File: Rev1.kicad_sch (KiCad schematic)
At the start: 105 parts, among them J1 Conn_01x08_Socket, J10 Conn_01x08_Socket, J11 Conn_01x02_Socket, J12 Conn_01x08_Socket, J13 Conn_01x08_Socket, J2 Conn_01x08_Socket, J3 Conn_01x08_Socket, J4 Conn_01x08_Socket, J5 Conn_01x08_Socket, J6 Conn_01x08_Socket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

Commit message: Update, pics
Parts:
- J11: value Conn_01x02_Socket -> Power
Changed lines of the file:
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@@
 		(on_board yes)
 		(dnp no)
-		(fields_autoplaced yes)
 		(property "Reference" "J11"
 			(at 21.59 30.4799 0)
@@
 			)
 		)
-		(property "Value" "Conn_01x02_Socket"
-			(at 21.59 31.7499 0)
+		(property "Value" "Power"
+			(at 22.098 33.274 0)
 			(effects
 				(font
@@
 				)
 				(justify left)
-				(hide yes)
 			)
 		)

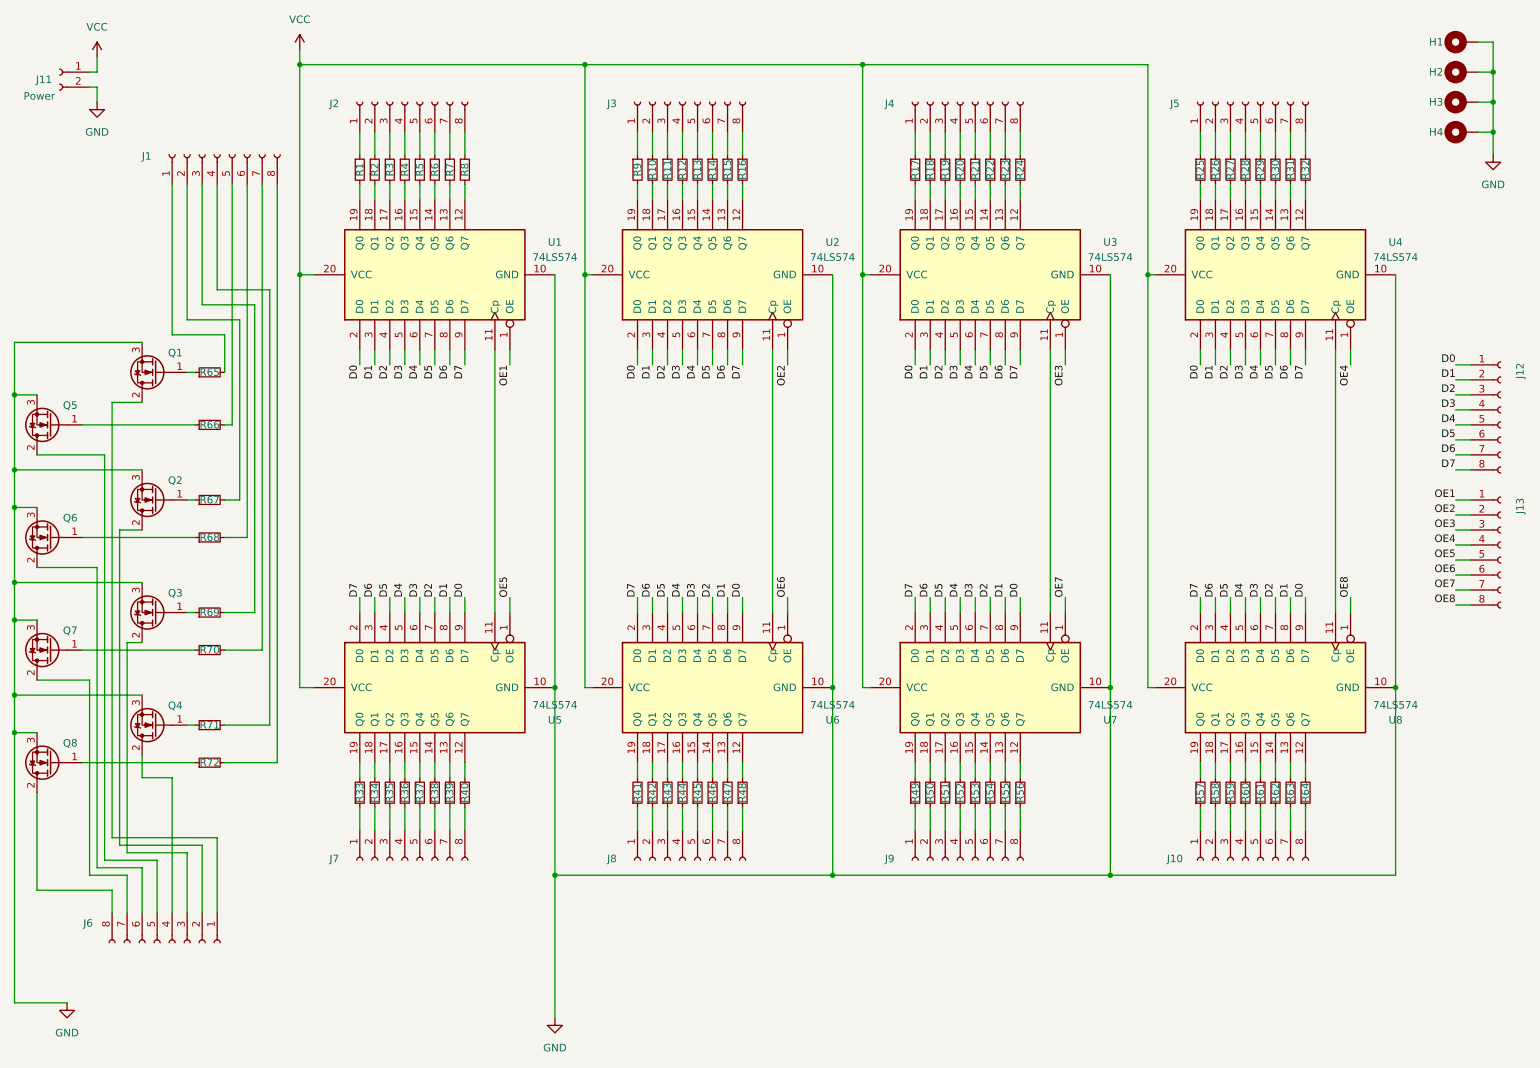
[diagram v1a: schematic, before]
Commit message: Added decoupling caps. Rerouted
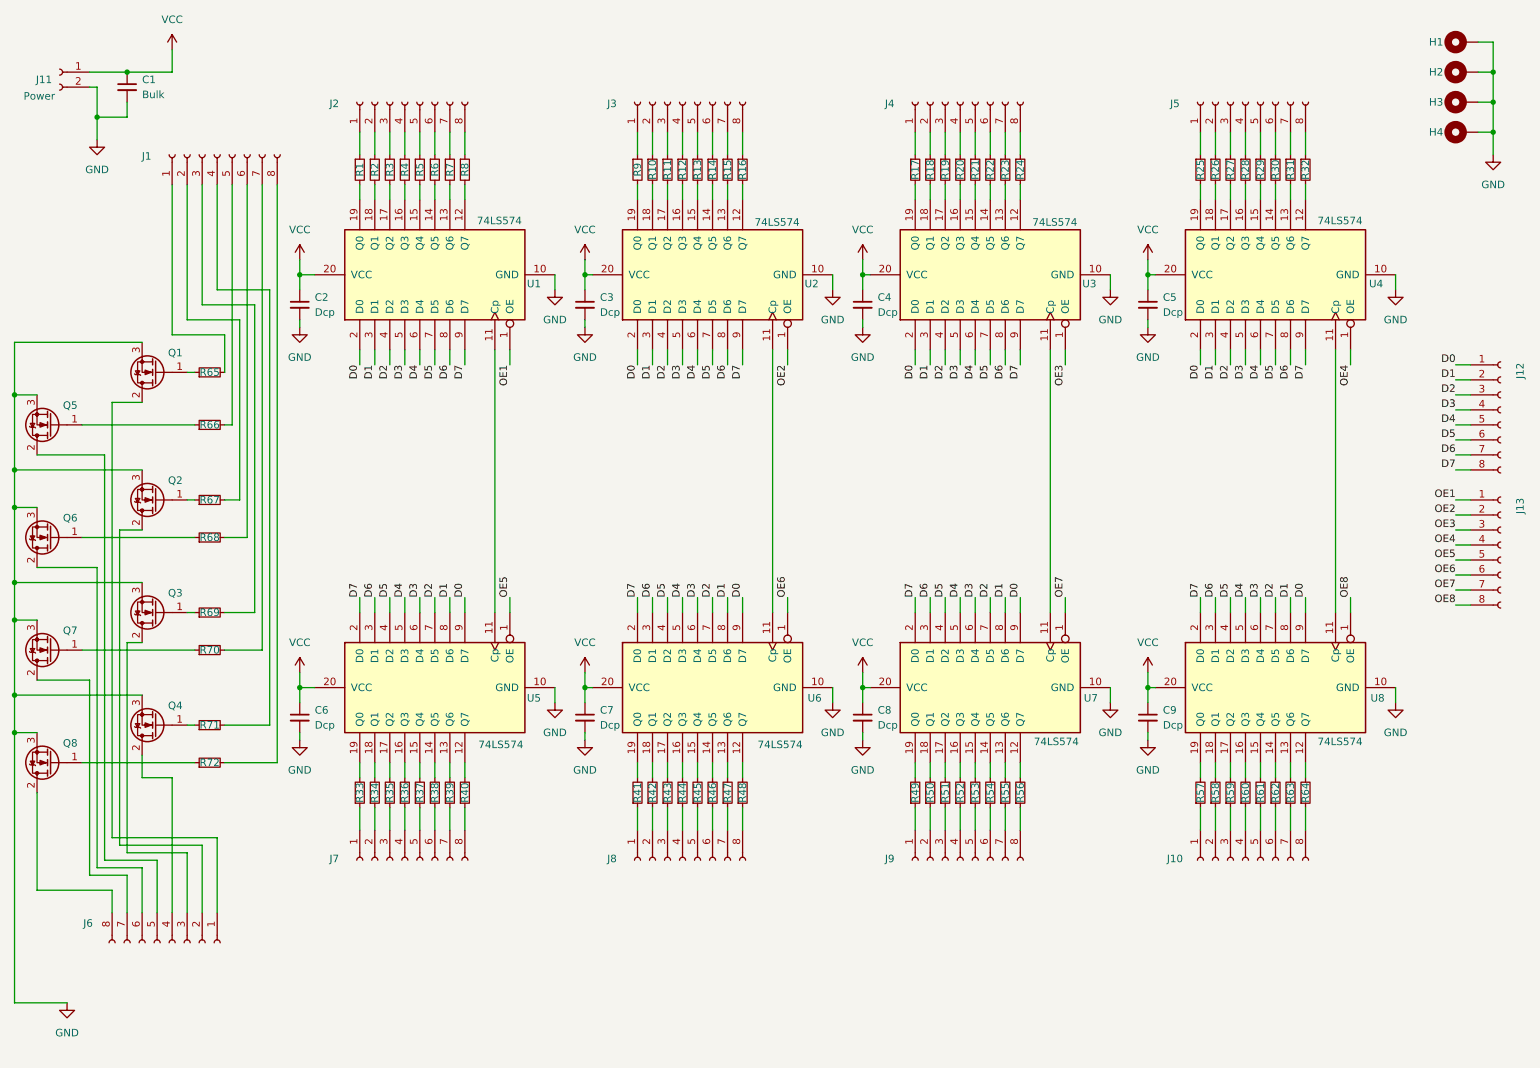
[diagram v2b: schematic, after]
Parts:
- added C1: Bulk, Capacitor_THT:C_Radial_D6.3mm_H7.0mm_P2.50mm, symbol Device:C_Small
- added C2, C3, C4, C5, C6, C7, C8, C9: Dcp, Capacitor_THT:C_Disc_D3.0mm_W2.0mm_P2.50mm, symbol Device:C_Small
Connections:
- net GND: now also C1.2, C2.2, C3.2, C4.2, C5.2, C6.2, C7.2, C8.2, C9.2
- net VCC: now also C1.1, C2.1, C3.1, C4.1, C5.1, C6.1, C7.1, C8.1, C9.1
